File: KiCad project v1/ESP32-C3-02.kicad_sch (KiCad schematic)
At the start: 20 parts, among them U3 ESP32-C3-WROOM-02-H4, U4 CP2102N-Axx-xQFN20

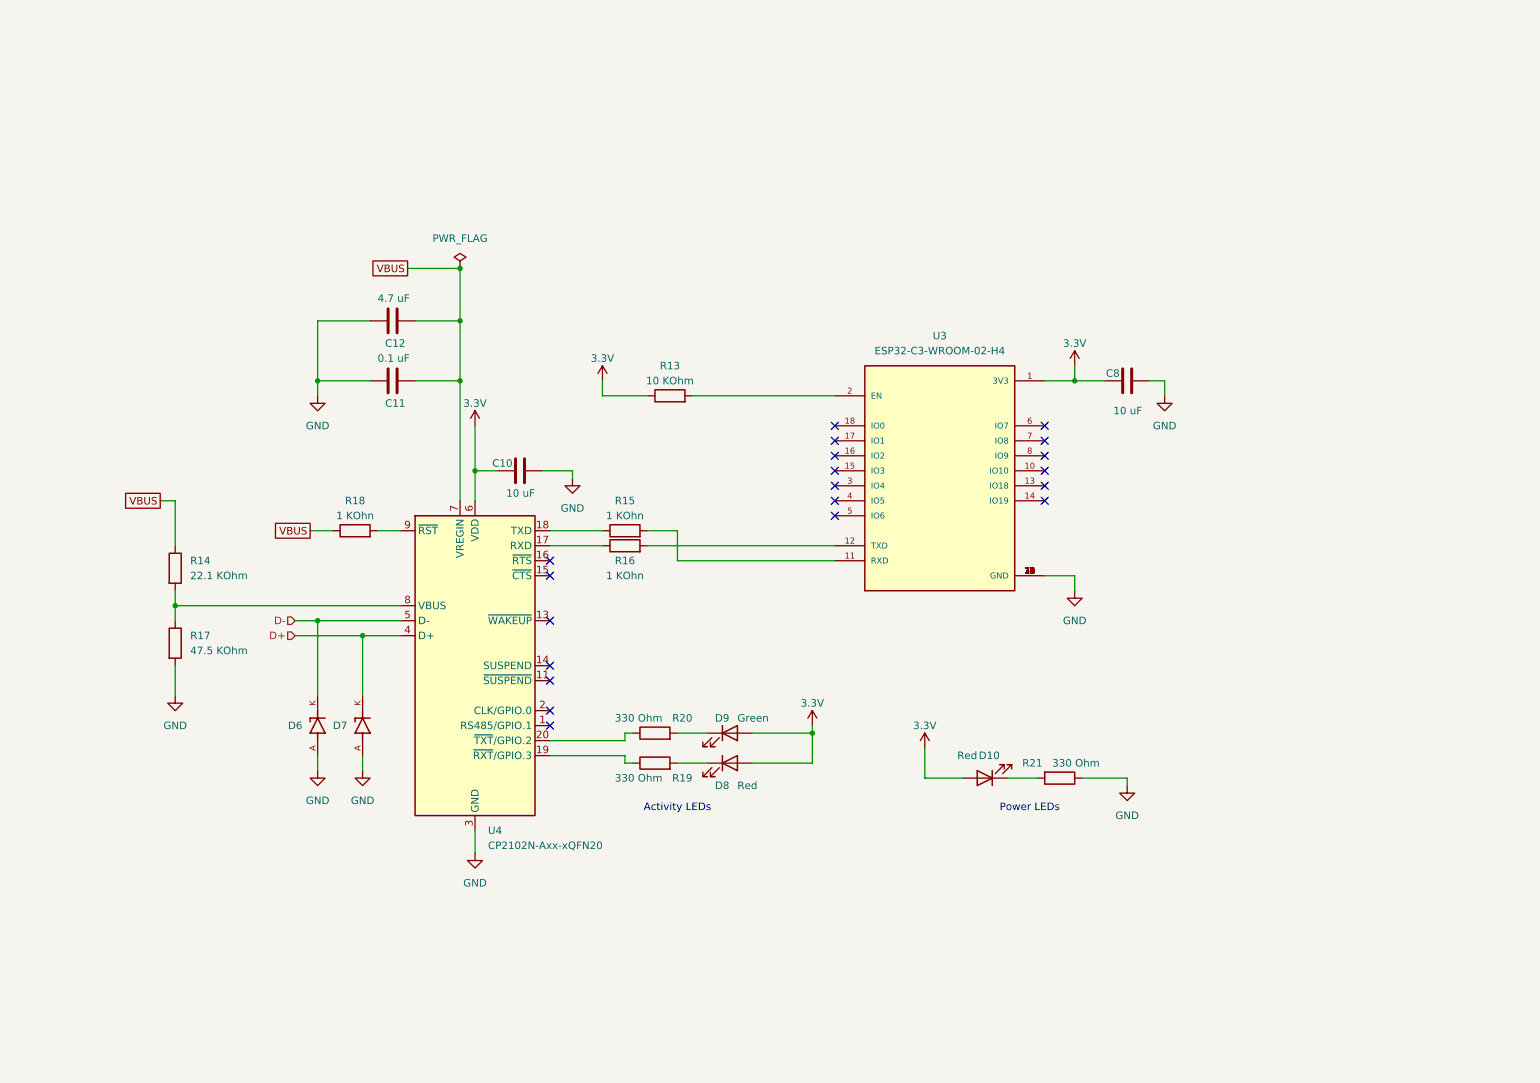
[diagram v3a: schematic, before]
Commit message: Added flash memory module and microsd module to the designed. Moved the libraries and datasheets in the project folder.
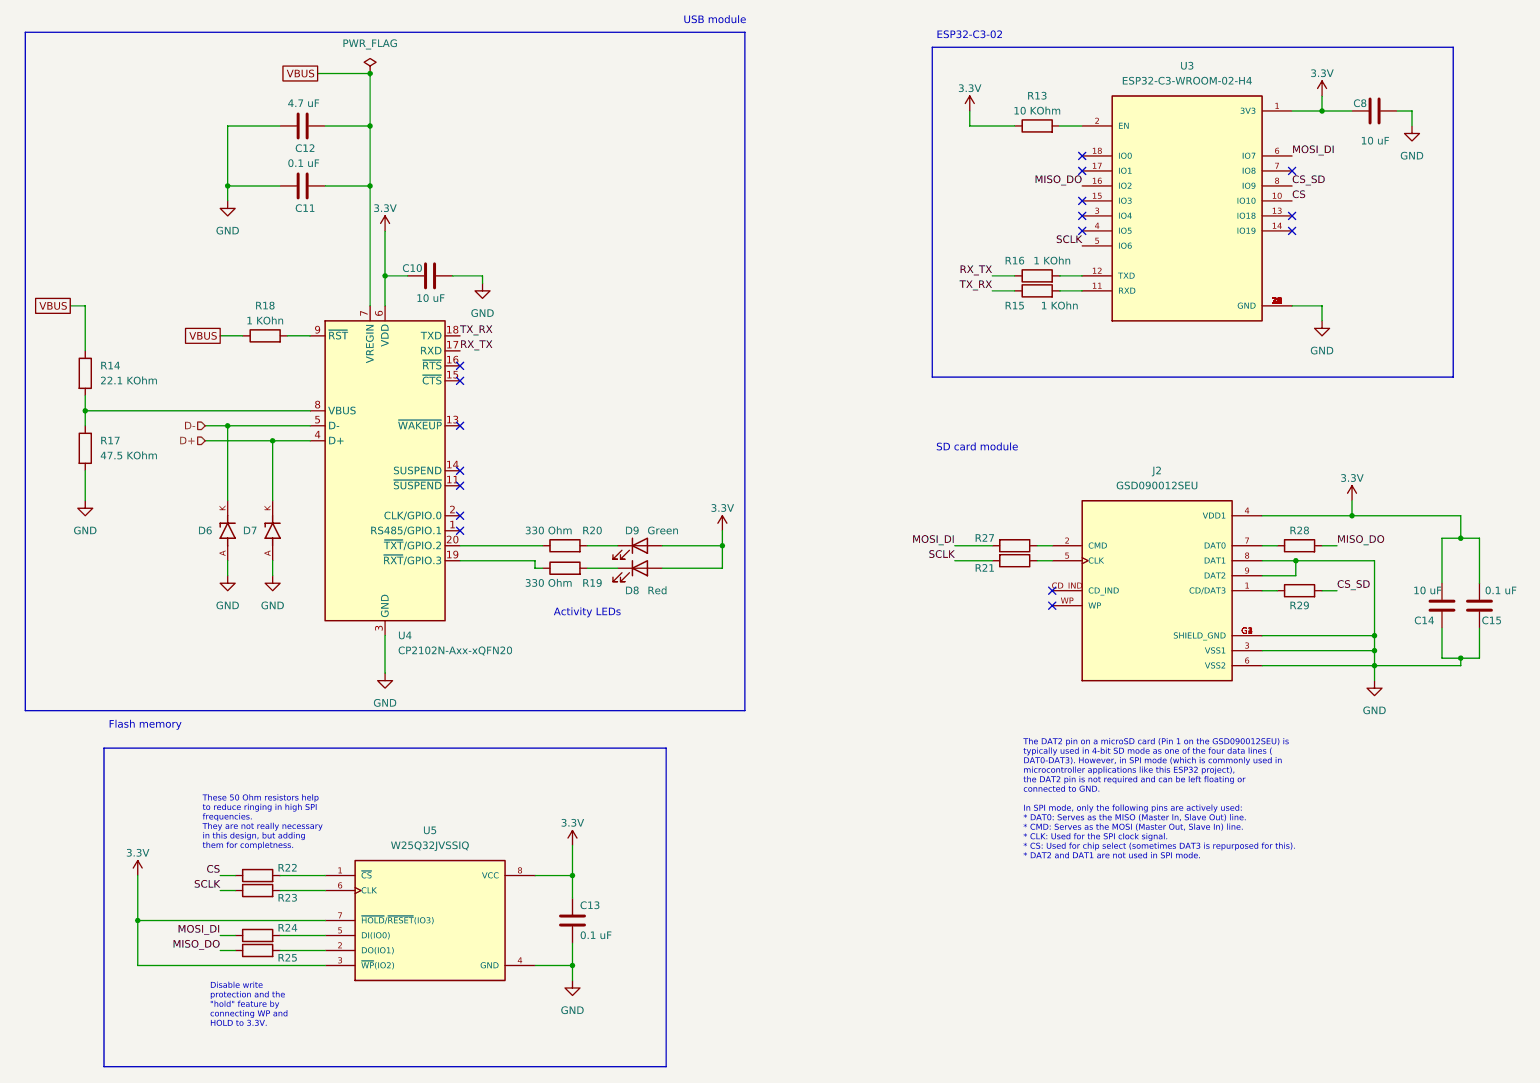
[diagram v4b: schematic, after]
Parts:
- removed D10: Red, SparkFun-LED:LED_0603_1608Metric, symbol SparkFun-LED:LED_Red_0603
- added C13, C15: 0.1 uF, Capacitor_SMD:C_0805_2012Metric, symbol SparkFun-Capacitor:C
- added C14: 10 uF, Capacitor_SMD:C_0805_2012Metric, symbol SparkFun-Capacitor:C
- added J2: GSD090012SEU, GSD090012SEU:AMPHENOL_GSD090012SEU, symbol GSD090012SEU:GSD090012SEU
- added R22, R23, R24, R25, R27, R28, R29: 50 Ohm, symbol Device:R
- added U5: W25Q32JVSSIQ, W25Q32JVSSIQ:SOIC127P790X216-8N, symbol W25Q32JVSSIQ:W25Q32JVSSIQ
- R21: value 330 Ohm -> 50 Ohm; footprint Resistor_SMD:R_0805_2012Metric -> (none); Purpose Current limiting -> Help reduce ringing in high-speed SPI.
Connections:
- net 3.3V: now also C13.1, C14.2, C15.2, J2.4 (VDD1), U5.3 (~{WP}(IO2)), U5.7 (~{HOLD}/~{RESET}(IO3)), U5.8 (VCC)
- net GND: now also C13.2, C14.1, C15.1, J2.3 (VSS1), J2.6 (VSS2), J2.8 (DAT1), J2.9 (DAT2), J2.G1 (SHIELD_GND), J2.G2 (SHIELD_GND), J2.G3 (SHIELD_GND), J2.G4 (SHIELD_GND), U5.4 (GND); no longer R21.1
- net SCLK: now reaches R21.2
- net SCLK: now also U3.5 (IO6), R23.1
- net TX_RX: now reaches R15.1, U4.18 (TXD)
- net RX_TX: now reaches R16.1, U4.17 (RXD)
- net CS: now reaches U3.10 (IO10)
- net CS: now also R22.1
- net MISO_DO: now reaches U3.16 (IO2)
- net MISO_DO: now also R25.1, R28.2
- net MOSI_DI: now reaches U3.6 (IO7)
- net MOSI_DI: now also R24.1, R27.2
- net CS_SD: now reaches U3.8 (IO9)
- net CS_SD: now also R29.2
- new net: J2.2 (CMD), R27.1
- new net: R25.2, U5.2 (DO(IO1))
- new net: J2.5 (CLK), R21.1
- new net: J2.7 (DAT0), R28.1
- new net: R22.2, U5.1 (~{CS})
- new net: R23.2, U5.6 (CLK)
- new net: J2.1 (CD/DAT3), R29.1
- new net: R24.2, U5.5 (DI(IO0))
- no-connect marks 20 -> 17
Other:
- note added: "ESP32-C3-02"
- note added: "Flash memory"
- note added: "SD card module"
- note added: "USB module"
- note removed: "Power LEDs"
- moved on the sheet: C10, C11, C12, C8, D6, D7, D8, D9, R13, R14, R15, R16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

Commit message: Added sensors to the schematic design.
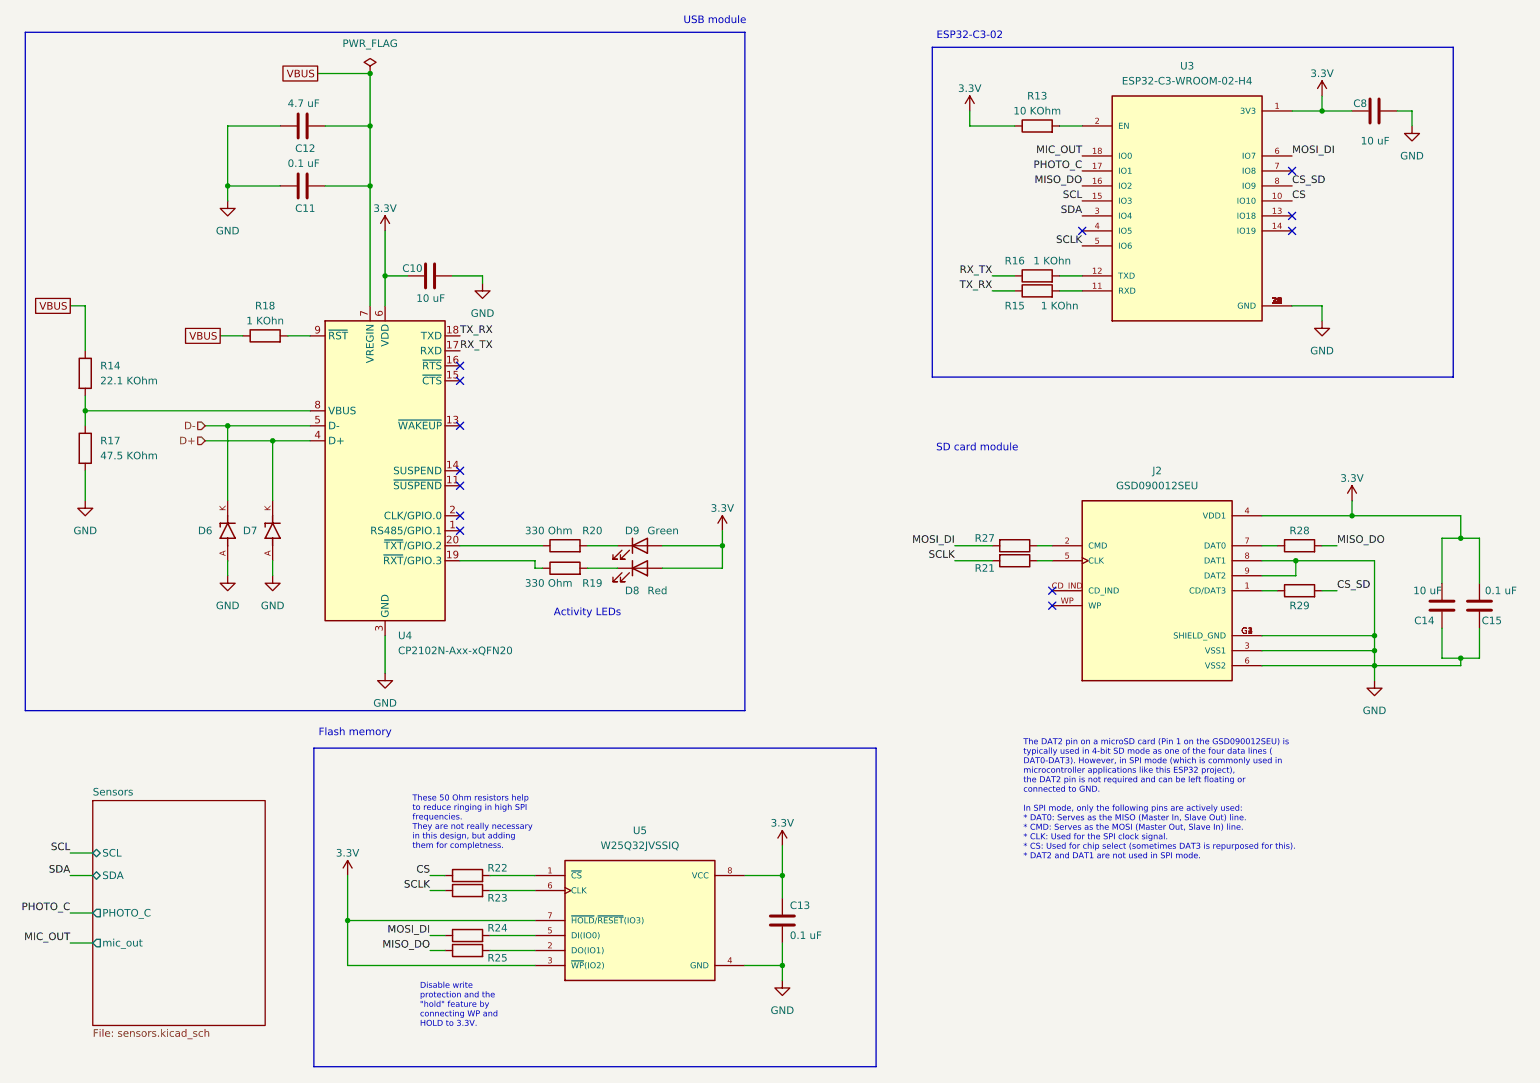
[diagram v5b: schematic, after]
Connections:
- net SCL: now reaches U3.15 (IO3)
- net PHOTO_C: now reaches U3.17 (IO1)
- net MIC_OUT: now reaches U3.18 (IO0)
- net SDA: now reaches U3.3 (IO4)
- no-connect marks 17 -> 13
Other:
- added sheet Sensors (sensors.kicad_sch)
- moved on the sheet: C13, R22, R23, R24, R25, U5

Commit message: Added an OLED I2C display connector, boot and reset buttons, and breakout for remaining pins.
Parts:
- removed R13: 10 KOhm, Resistor_SMD:R_0805_2012Metric, symbol Device:R
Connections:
- net MIC_OUT: now also U3.4 (IO5); no longer U3.18 (IO0)
- net EN: now reaches U3.2 (EN)
- net DTS: now reaches U4.15 (~{CTS})
- net RTS: now reaches U4.16 (~{RTS})
- net GPIO18: now reaches U3.13 (IO18)
- net GPIO19: now reaches U3.14 (IO19)
- net GPIO8: now reaches U3.7 (IO8)
- new net BOOT: U3.18 (IO0)
- no-connect marks 13 -> 7
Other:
- added sheet User interface (user_interface.kicad_sch)
- moved on the sheet: C13, R22, R23, R24, R25, U5

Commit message: Completed symbol and footprint associations.
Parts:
- R21, R22, R23, R24, R25, R27, R28, R29: footprint (none) -> Resistor_SMD:R_0201_0603Metric
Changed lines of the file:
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@@
 			)
 		)
-		(property "Footprint" ""
+		(property "Footprint" "Resistor_SMD:R_0201_0603Metric"
 			(at 191.77 101.092 90)
 			(effects
@@
 			)
 		)
-		(property "Footprint" ""
+		(property "Footprint" "Resistor_SMD:R_0201_0603Metric"
 			(at 50.8 170.688 90)
 			(effects
@@
 			)
 		)
-		(property "Footprint" ""
+		(property "Footprint" "Resistor_SMD:R_0201_0603Metric"
 			(at 191.77 103.632 90)
 			(effects
@@
 			)
 		)
-		(property "Footprint" ""
+		(property "Footprint" "Resistor_SMD:R_0201_0603Metric"
 			(at 240.03 104.648 90)
 			(effects
@@
 			)
 		)
-		(property "Footprint" ""
+		(property "Footprint" "Resistor_SMD:R_0201_0603Metric"
 			(at 50.8 157.988 90)
 			(effects
@@
 			)
 		)
-		(property "Footprint" ""
+		(property "Footprint" "Resistor_SMD:R_0201_0603Metric"
 			(at 50.8 160.528 90)
 			(effects
@@
 			)
 		)
-		(property "Footprint" ""
+		(property "Footprint" "Resistor_SMD:R_0201_0603Metric"
 			(at 50.8 168.148 90)
 			(effects
@@
 			)
 		)
-		(property "Footprint" ""
+		(property "Footprint" "Resistor_SMD:R_0201_0603Metric"
 			(at 240.03 112.268 90)
 			(effects

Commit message: Small fixes.
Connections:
- net D+ renamed USB_DP
- net D- renamed USB_DN
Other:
- sheet Sensors ports: added MIC_OUT; removed mic_out
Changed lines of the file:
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@@
 	)
 	(junction
-		(at 267.335 101.6)
+		(at 267.97 101.6)
 		(diameter 0)
 		(color 0 0 0 0)
@@
 	)
 	(junction
-		(at 267.335 121.92)
+		(at 267.97 121.92)
 		(diameter 0)
 		(color 0 0 0 0)
@@
 	)
 	(junction
-		(at 239.395 105.41)
+		(at 240.03 105.41)
 		(diameter 0)
 		(color 0 0 0 0)
@@
 	(wire
 		(pts
-			(xy 270.51 101.6) (xy 267.335 101.6)
+			(xy 270.51 101.6) (xy 267.97 101.6)
 		)
 		(stroke
@@
 	(wire
 		(pts
-			(xy 267.335 121.92) (xy 270.51 121.92)
+			(xy 267.97 121.92) (xy 270.51 121.92)
 		)
 		(stroke
@@
 	(wire
 		(pts
-			(xy 239.395 107.95) (xy 239.395 105.41)
+			(xy 240.03 107.95) (xy 240.03 105.41)
 		)
 		(stroke
@@
 	(wire
 		(pts
-			(xy 267.335 97.79) (xy 267.335 101.6)
+			(xy 267.97 97.79) (xy 267.97 101.6)
 		)
 		(stroke
@@
 	(wire
 		(pts
-			(xy 233.68 105.41) (xy 239.395 105.41)
+			(xy 233.68 105.41) (xy 240.03 105.41)
 		)
 		(stroke
@@
 	(wire
 		(pts
-			(xy 248.92 97.79) (xy 267.335 97.79)
+			(xy 248.92 97.79) (xy 267.97 97.79)
 		)
 		(stroke
@@
 	(wire
 		(pts
-			(xy 264.16 121.92) (xy 267.335 121.92)
+			(xy 264.16 121.92) (xy 267.97 121.92)
 		)
 		(stroke
@@
 	(wire
 		(pts
-			(xy 267.335 123.19) (xy 252.73 123.19)
+			(xy 267.97 123.19) (xy 252.73 123.19)
 		)
 		(stroke
@@
 	(wire
 		(pts
-			(xy 267.335 101.6) (xy 264.16 101.6)
+			(xy 267.97 101.6) (xy 264.16 101.6)
 		)
 		(stroke
@@
 	(wire
 		(pts
-			(xy 267.335 121.92) (xy 267.335 123.19)
+			(xy 267.97 121.92) (xy 267.97 123.19)
 		)
 		(stroke
@@
 	(wire
 		(pts
-			(xy 233.68 107.95) (xy 239.395 107.95)
+			(xy 233.68 107.95) (xy 240.03 107.95)
 		)
 		(stroke
@@
 	(wire
 		(pts
-			(xy 239.395 105.41) (xy 252.73 105.41)
+			(xy 240.03 105.41) (xy 252.73 105.41)
 		)
 		(stroke
@@
 		)
 	)
-	(hierarchical_label "D+"
+	(hierarchical_label "USB_DP"
 		(shape input)
 		(at 54.61 85.09 180)
@@
 		)
 	)
-	(hierarchical_label "D-"
+	(hierarchical_label "USB_DN"
 		(shape input)
 		(at 54.61 82.55 180)
@@
 			)
 		)
-		(pin "mic_out" output
+		(pin "MIC_OUT" output
 			(at 138.43 154.94 180)
 			(effects
